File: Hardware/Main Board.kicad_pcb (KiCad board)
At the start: 2 copper layers, 64 parts, among them J1 Conn_RJ-45, J2 Conn_RJ-45, J3 Conn_RJ-45, J4 Conn_RJ-45, P1 Load_Cell_Conn, P2 ST_SWD_Connector, P3 BATT, U1 STM32F401RCT6, U2 SN75176BDR, U3 AOZ1280CI, U4 AP65552SP-13, X1 24MHz

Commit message: Layout of PCB
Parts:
- GPS1: footprint MAVRIC:GPS -> MAVRIc:GPS_Pads
- moved R5 105.2 mm to (161.3, 80.8), turned to 270 degrees
- moved R8 92.8 mm to (135.4, 73.7)
- moved C4 83.2 mm to (116.6, 122.6)
- moved C5 82.2 mm to (116.6, 126.0)
- moved C6 81.3 mm to (116.6, 129.3)
- moved C8 80.3 mm to (116.6, 132.6)
- moved R14 76.3 mm to (117.9, 72.1)
- moved C14 76.0 mm to (100.6, 99.6), turned to 90 degrees
- moved ADC1 74.8 mm to (138.0, 109.7), turned to 270 degrees
- moved BTA1 73.2 mm to (163.5, 59.3)
- moved BTA2 73.2 mm to (138.7, 59.1)
- moved J1 73.2 mm to (173.9, 63.3)
- moved P2 73.2 mm to (140.5, 74.3)
- moved C1 73.2 mm to (143.9, 82.1)
- moved GP1 73.2 mm to (158.1, 92.7)
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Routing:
- net /Regulator +3v3/Reg+3v3: track 0.00 -> 121.7 mm, vias 0 -> 4
- net /RS485OUT/485_A_OUT: track 0.00 -> 63.1 mm, vias 0 -> 4
- net /RS485OUT/485_B_OUT: track 0.00 -> 60.8 mm, vias 0 -> 2
- net /Regulator +3v3/REG2EN: track 0.00 -> 57.6 mm, vias 0 -> 2
- net /Vernier Sensors Module/ANA1: track 0.00 -> 46.6 mm, vias 0 -> 2
- net /Vernier Sensors Module/ANA2: track 0.00 -> 38.0 mm, vias 0 -> 2
- net Net-(U1-Pad41): track 1.27 -> 30.7 mm, vias 0 -> 2
- net /RS485OUT/USART1_TX_OUT: track 34.0 -> 61.7 mm, vias 0 -> 2
- net /OSC_OUT: track 7.21 -> 32.5 mm
- net /NRST: track 0.00 -> 25.1 mm, vias 0 -> 2
- net /SWDIO: track 0.00 -> 24.2 mm, vias 0 -> 2
- net /GPS_RX: track 0.00 -> 23.8 mm, vias 0 -> 2
- net Net-(C14-Pad2): track 0.00 -> 23.3 mm
- net /GPS_TX: track 0.00 -> 23.0 mm, vias 0 -> 2
- net /GPIO2: track 0.00 -> 22.0 mm
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
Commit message: PCB Almost Complete
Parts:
- added C24: 4.7uF, Capacitors_SMD:C_1206_HandSoldering, F.Cu at (101.0, 89.3)
- added ISU MAVRIC: VAL**, MAVRIc:MAVRIC_LOGO, F.Cu at (103.4, 135.8)
- R12: value 191k -> 124k
- moved L1 17.5 mm to (98.6, 104.9), turned to 270 degrees
- moved C21 17.3 mm to (112.7, 85.0), turned to 180 degrees
- moved C19 17.0 mm to (112.7, 82.1)
- moved C10 12.9 mm to (128.0, 109.7)
- moved C4 12.9 mm to (118.1, 109.7)
- moved C11 12.9 mm to (128.0, 113.2)
- moved C12 12.9 mm to (128.0, 116.5)
- moved C13 12.9 mm to (128.0, 119.8)
- moved C5 12.9 mm to (118.1, 113.2)
- moved C6 12.9 mm to (118.1, 116.5)
- moved C8 12.9 mm to (118.1, 119.8)
- moved C9 12.9 mm to (128.0, 106.0)
- moved C3 11.9 mm to (120.7, 92.3)
- moved C7 11.9 mm to (120.7, 100.1)
- moved X1 11.9 mm to (127.5, 96.4)
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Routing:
- net GND: track 13.7 -> 365.4 mm, vias 0 -> 10
- net /RS485OUT/Reg+5V: track 0.00 -> 115.8 mm, vias 0 -> 2
- net +12V: track 16.5 -> 124.6 mm, vias 0 -> 4
- net /ADC1_IN2: track 0.00 -> 53.4 mm, vias 0 -> 2
- net /Regulator +3v3/REG2EN: track 57.6 -> 12.6 mm
- net Net-(R1-Pad1): track 9.18 -> 31.5 mm, vias 0 -> 2
- net /Regulator +3v3/Reg+3v3: track 121.7 -> 105.4 mm, vias 4 -> 2
- net Net-(R4-Pad2): track 6.60 -> 18.7 mm
- net /OSC_OUT: track 32.5 -> 23.2 mm
- net Net-(C14-Pad2): track 23.3 -> 15.1 mm
- net /OSC_IN: track 24.0 -> 18.2 mm
- net Net-(C18-Pad1): track 0.00 -> 4.06 mm
- net Net-(C22-Pad2): track 11.9 -> 8.19 mm
- net Net-(C22-Pad1): track 7.24 -> 3.91 mm
- net Net-(C14-Pad1): track 8.50 -> 5.58 mm
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- added copper zone on F.Cu, net (none)
- added copper zone on F.Cu, net +12V
- added copper zone on F.Cu, net /RS485OUT/Reg+5V
- added copper zone on F.Cu, net GND
- added copper zone on F.Cu, net Net-(C22-Pad2)
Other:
- board text added: "Main Board"

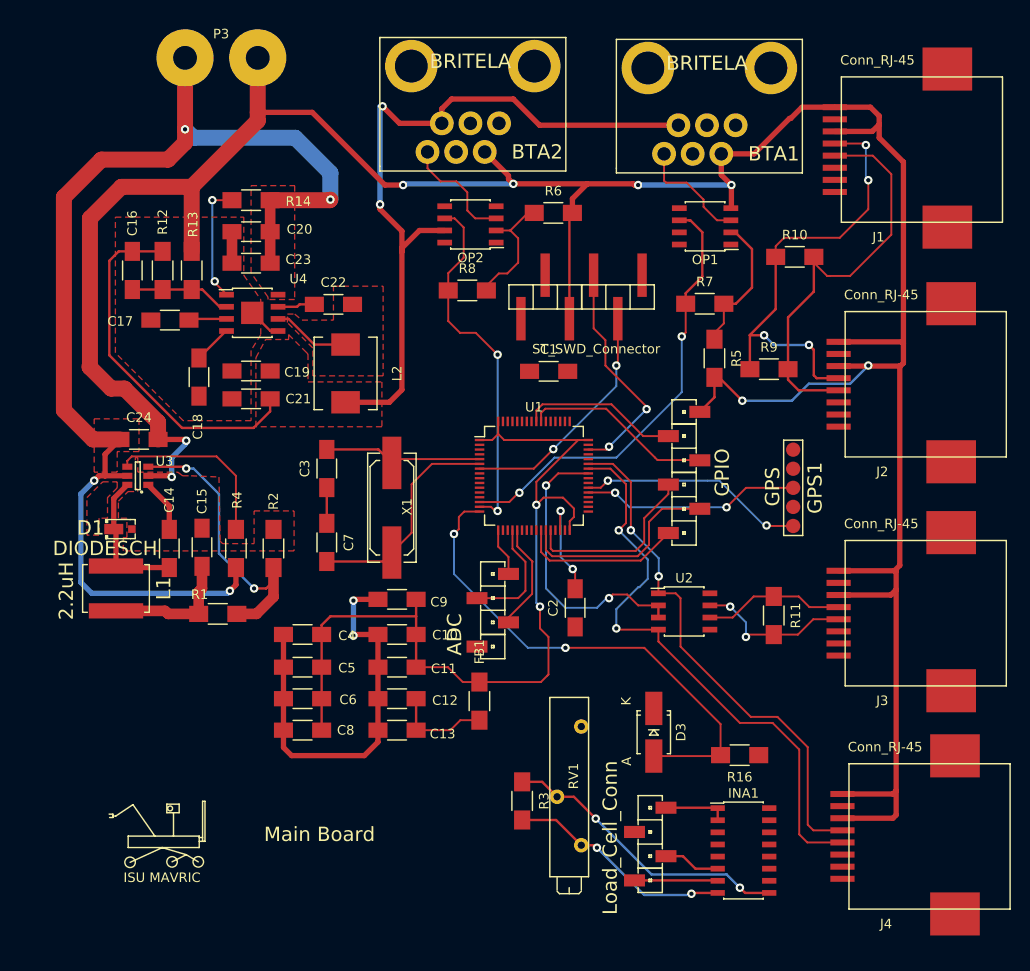
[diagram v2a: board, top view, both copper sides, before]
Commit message: Add ground Plane
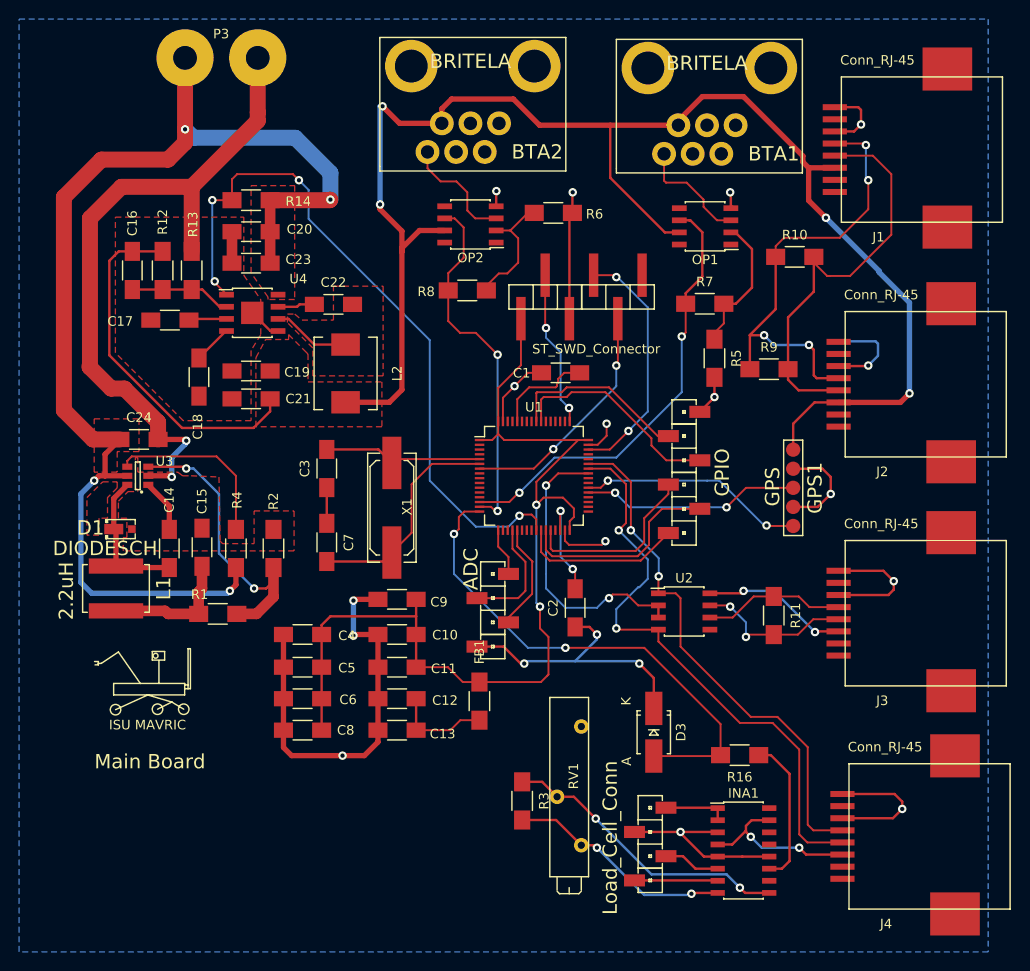
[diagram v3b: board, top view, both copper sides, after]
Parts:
- moved ISU MAVRIC 16.1 mm to (101.9, 119.8)
- moved C1 1.26 mm to (145.2, 82.3)
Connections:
- RV1 pad 1: GND -> Net-(RV1-Pad1)
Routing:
- net /RS485OUT/Reg+5V: track 115.8 -> 230.0 mm, vias 2 -> 8
- net GND: track 365.4 -> 266.9 mm, vias 10 -> 21
- net /Regulator +3v3/REG2EN: track 12.6 -> 74.5 mm, vias 2 -> 4
- net /SWCLK: track 0.00 -> 16.4 mm, vias 0 -> 2
- net Net-(INA1-Pad10): track 0.00 -> 16.2 mm
- net /Regulator +3v3/Reg+3v3: track 105.4 -> 117.2 mm
- net Net-(C1-Pad2): track 0.00 -> 10.4 mm
- net /GPIO4: track 20.0 -> 22.7 mm
- net /GPIO5: track 16.6 -> 19.2 mm
- net /SWDIO: track 24.2 -> 25.9 mm
- added copper zone on B.Cu, net GND

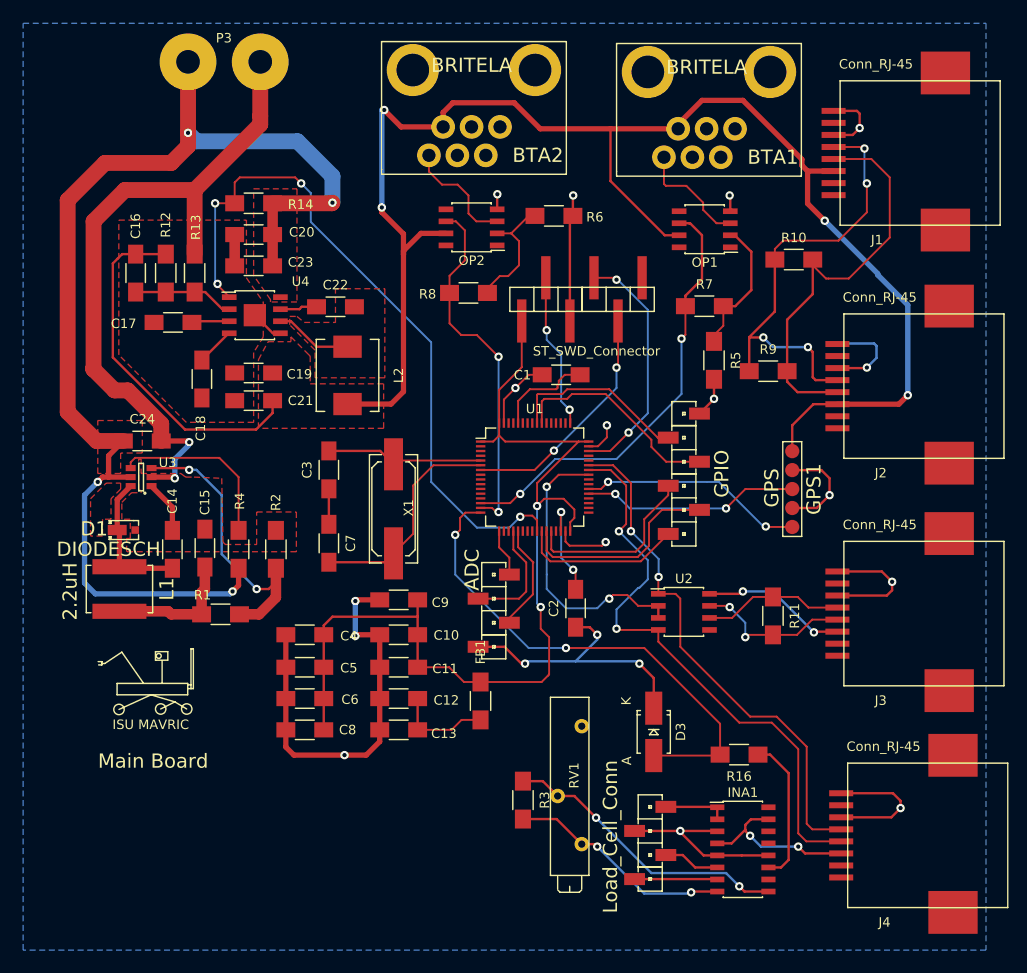
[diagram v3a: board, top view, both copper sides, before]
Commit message: Main Board Finished
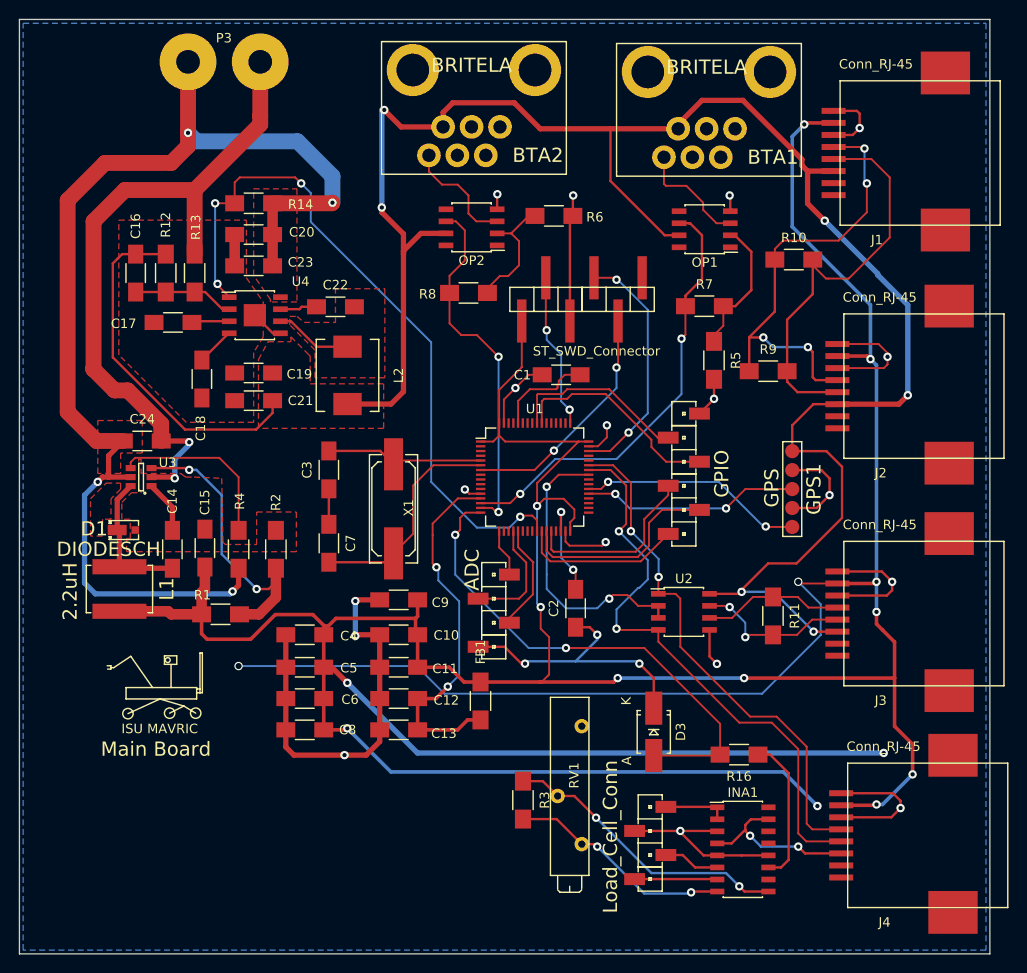
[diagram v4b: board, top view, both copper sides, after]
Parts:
- moved ISU MAVRIC 1.04 mm to (102.8, 120.2)
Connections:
- C10 pad 2: /Regulator +3v3/Reg+3v3 -> /RS485OUT/Reg+3V3
- C11 pad 2: /Regulator +3v3/Reg+3v3 -> /RS485OUT/Reg+3V3
- C15 pad 2: /Regulator +3v3/Reg+3v3 -> /RS485OUT/Reg+3V3
- C4 pad 2: /Regulator +3v3/Reg+3v3 -> /RS485OUT/Reg+3V3
- C5 pad 2: /Regulator +3v3/Reg+3v3 -> /RS485OUT/Reg+3V3
- C6 pad 2: /Regulator +3v3/Reg+3v3 -> /RS485OUT/Reg+3V3
- C8 pad 2: /Regulator +3v3/Reg+3v3 -> /RS485OUT/Reg+3V3
- C9 pad 2: /Regulator +3v3/Reg+3v3 -> /RS485OUT/Reg+3V3
- FB1 pad 1: /Regulator +3v3/Reg+3v3 -> /RS485OUT/Reg+3V3
- J1 pad 7: /RS485OUT/Reg+3v3 -> /RS485OUT/Reg+3V3
- J2 pad 7: /RS485OUT/Reg+3v3 -> /RS485OUT/Reg+3V3
- J3 pad 7: /RS485OUT/Reg+3v3 -> /RS485OUT/Reg+3V3
- J4 pad 7: /RS485OUT/Reg+3v3 -> /RS485OUT/Reg+3V3
- L1 pad 2: /Regulator +3v3/Reg+3v3 -> /RS485OUT/Reg+3V3
- P2 pad 1: /Regulator +3v3/Reg+3v3 -> /RS485OUT/Reg+3V3
- R1 pad 2: /Regulator +3v3/Reg+3v3 -> /RS485OUT/Reg+3V3
- U1 pad 1: /Regulator +3v3/Reg+3v3 -> /RS485OUT/Reg+3V3
- U1 pad 19: /Regulator +3v3/Reg+3v3 -> /RS485OUT/Reg+3V3
- U1 pad 32: /Regulator +3v3/Reg+3v3 -> /RS485OUT/Reg+3V3
- U1 pad 48: /Regulator +3v3/Reg+3v3 -> /RS485OUT/Reg+3V3
- U1 pad 64: /Regulator +3v3/Reg+3v3 -> /RS485OUT/Reg+3V3
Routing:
- net /RS485OUT/Reg+3V3: track 0.00 -> 460.1 mm, vias 0 -> 16
- net /Regulator +3v3/Reg+3v3: track 117.2 -> 0.00 mm, vias 2 -> 0
- net /VDDA: track 10.3 -> 41.0 mm, vias 0 -> 2
- net /RS485OUT/Reg+5V: track 230.0 -> 255.7 mm
- net GND: track 266.9 -> 276.1 mm, vias 21 -> 23
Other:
- board outline added: 102.4 x 98.6 mm
- net class Default: clearance 0.254 -> 0.2032; trace_width 0.254 -> 0.2032
- rule trace_clearance: 0.254 -> 0.2032
